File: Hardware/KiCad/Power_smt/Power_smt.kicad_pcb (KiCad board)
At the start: 2 copper layers, 38.1 x 25.4 mm, 11 parts

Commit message: power board kicad smt
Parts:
- removed @HOLE0: , 
- removed D1: 1N5819-B, switched-lm2575:DO41-7.6
- removed R1: , switched-lm2575:0207_10
- added C3: 100nF, Capacitor_SMD:C_0805_2012Metric, F.Cu at (134.6, 101.6)
- added C4: 22uF, Capacitor_SMD:C_0805_2012Metric, F.Cu at (134.6, 104.6)
- C1: value 100uF -> 10uF; footprint switched-lm2575:E2,5-6 -> Capacitor_SMD:C_0805_2012Metric
- C2: value 330uF -> 22uF; footprint switched-lm2575:E3,5-8 -> Capacitor_SMD:C_0805_2012Metric
- GND0, UNK5V0: value (none) -> 3,81/1,4
- IC1: value (none) -> LM2596TV; footprint switched-lm2575:TO220-51 -> Package_TO_SOT_SMD:TSOT-23-6
- J1: value (none) -> JACK-PLUG0; footprint switched-lm2575:SPC4077 -> Connector_BarrelJack:BarrelJack_CUI_PJ-036AH-SMT_Horizontal
- JP1: value (none) -> PINHD-1X2; footprint switched-lm2575:1X02 -> Connector_PinHeader_2.54mm:PinHeader_1x02_P2.54mm_Vertical_SMD_Pin1Right
- L1: value 470uH -> 4.7uH; footprint switched-lm2575:SMCC12 -> Inductor_SMD:L_1008_2520Metric
- moved L1 24.3 mm to (134.6, 96.5)
- moved C2 13.1 mm to (139.7, 94.0)
- moved J1 5.07 mm to (157.5, 99.1), turned to 180 degrees
- moved C1 3.99 mm to (138.4, 101.6)
- moved IC1 3.95 mm to (144.8, 96.5)
- moved JP1 2.53 mm to (144.8, 104.1)
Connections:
- IC1 pad 1: VIN -> VCC
- IC1 pad 2: N$2 -> Net-(IC1-EN)
- IC1 pad 3: GND -> Net-(IC1-EN)
- IC1 pad 4: VCC -> GND
- IC1 pad 5: N$3 -> Net-(IC1-SW)
- J1 pad 2: (no net) -> unconnected-(J1-Pad2)
- J1 pad 3: VIN -> Net-(J1-Pad3)
- JP1 pad 1: N$3 -> Net-(J1-Pad3)
- JP1 pad 2: VIN -> Net-(IC1-EN)
- L1 pad 1: N$2 -> Net-(IC1-SW)
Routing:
- net VIN: track 65.4 -> 0.00 mm
- net VCC: track 33.9 -> 61.3 mm, vias 0 -> 3
- net Net-(IC1-SW): track 0.00 -> 27.2 mm, vias 0 -> 2
- net N$2: track 17.0 -> 0.00 mm
- net Net-(J1-Pad3): track 0.00 -> 16.0 mm
- net Net-(IC1-BST): track 0.00 -> 15.8 mm, vias 0 -> 2
- net Net-(IC1-EN): track 0.00 -> 15.6 mm
- net N$3: track 5.97 -> 0.00 mm

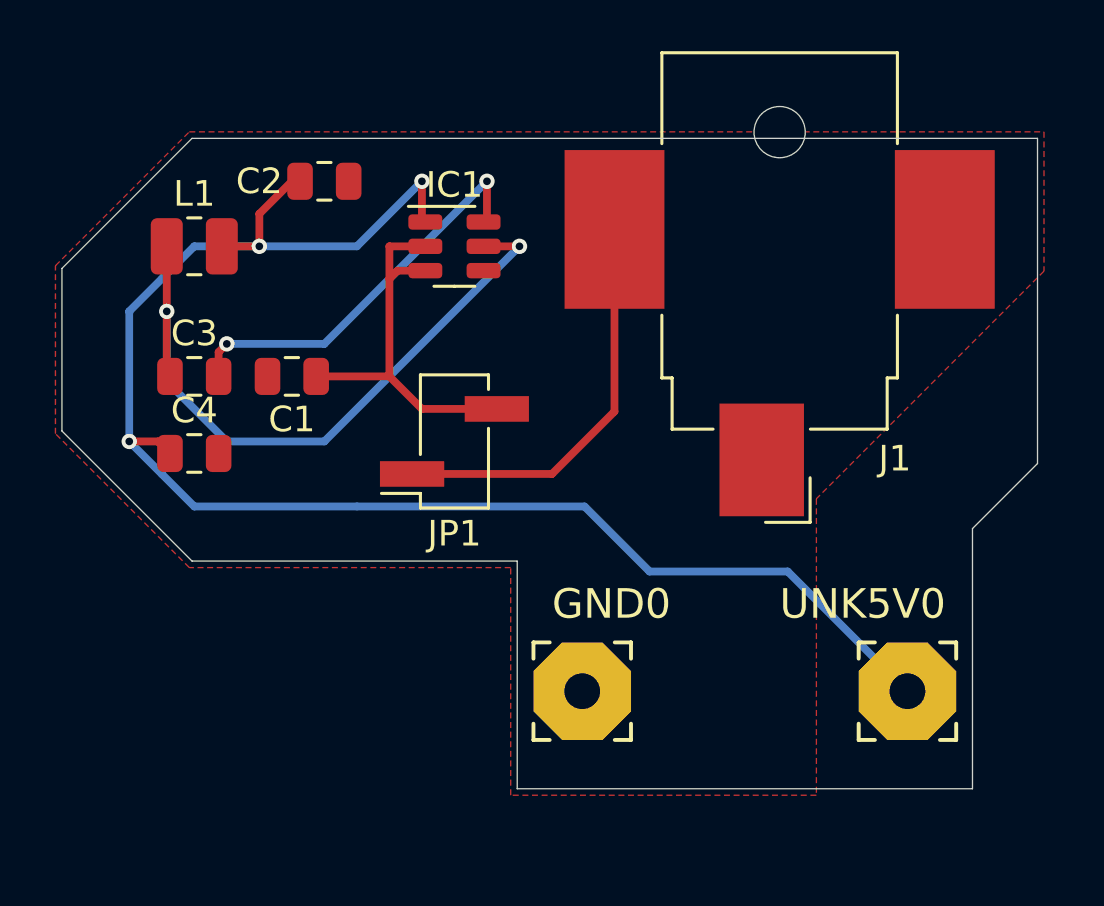
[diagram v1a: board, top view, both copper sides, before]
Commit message: SMT edits and start of fake dual ram sketching
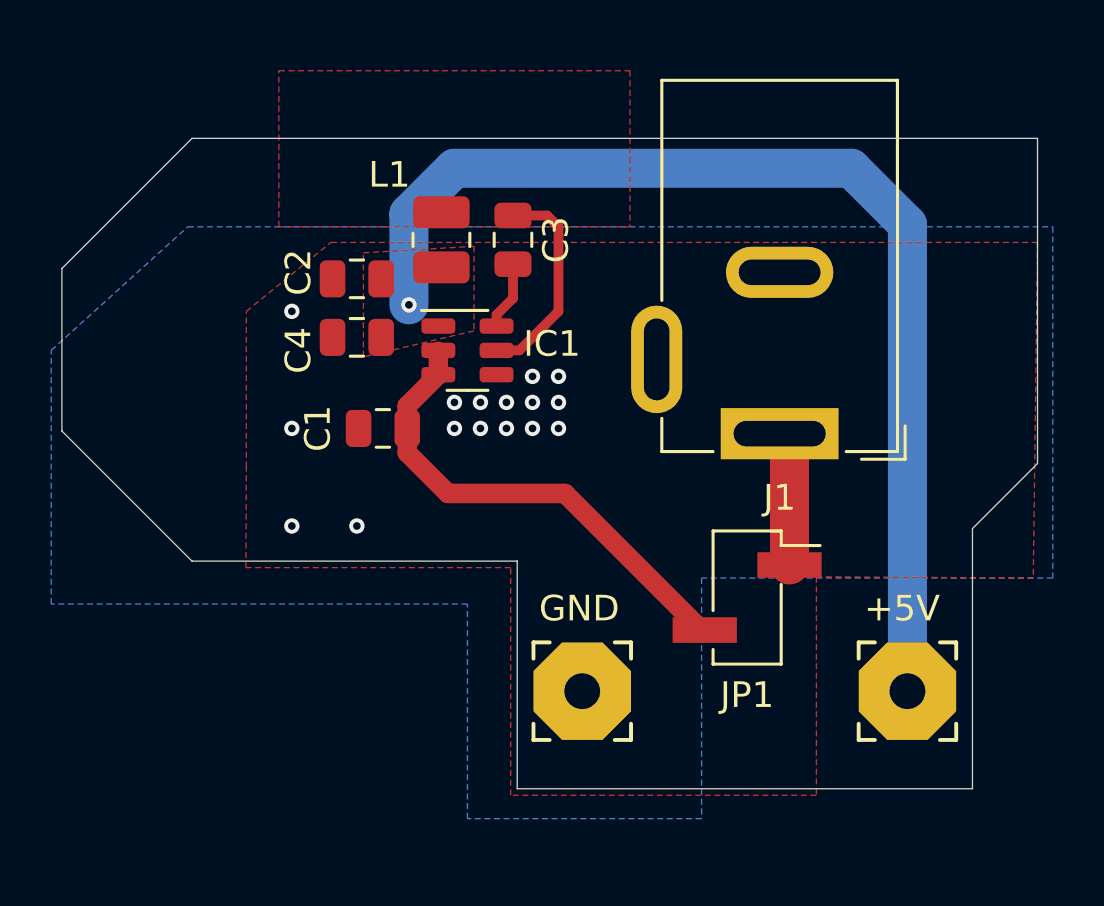
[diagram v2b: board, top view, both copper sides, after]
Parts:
- IC1: value LM2596TV -> AP63205WU-7
- J1: footprint Connector_BarrelJack:BarrelJack_CUI_PJ-036AH-SMT_Horizontal -> Connector_BarrelJack:BarrelJack_GCT_DCJ200-10-A_Horizontal
- moved C3 13.5 mm to (147.1, 96.3), turned to -90 degrees
- moved JP1 13.0 mm to (156.2, 110.2), turned to 0 degrees
- moved L1 9.66 mm to (144.3, 96.3), turned to -90 degrees
- moved C4 7.80 mm to (141.0, 100.1), turned to 180 degrees
- moved J1 4.78 mm to (157.5, 103.8)
- moved IC1 4.10 mm to (145.3, 100.6)
- moved C1 4.10 mm to (142.0, 103.6)
- moved C2 4.02 mm to (141.0, 97.8), turned to 180 degrees
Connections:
- J1 pad 1: GND -> Net-(J1-Pad1)
- J1 pad 2: unconnected-(J1-Pad2) -> GND
- J1 pad 3: Net-(J1-Pad3) -> unconnected-(J1-Pad3)
- JP1 pad 1: Net-(J1-Pad3) -> Net-(J1-Pad1)
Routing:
- net Net-(IC1-SW): track 27.2 -> 8.31 mm, vias 2 -> 0
- net VCC: track 61.3 -> 42.9 mm, vias 3 -> 1
- net Net-(J1-Pad3): track 16.0 -> 0.00 mm
- net Net-(IC1-BST): track 15.8 -> 2.68 mm, vias 2 -> 0
- net Net-(J1-Pad1): track 0.00 -> 5.29 mm
- net Net-(IC1-EN): track 15.6 -> 18.8 mm
- net GND: vias 0 -> 16
- added copper zone on B.Cu, net GND
- added copper zone on F.Cu, net Net-(IC1-SW)
- added copper zone on F.Cu, net VCC
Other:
- board text added: "+5V"
- board text added: "GND"

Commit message: updates to kicad smt versions
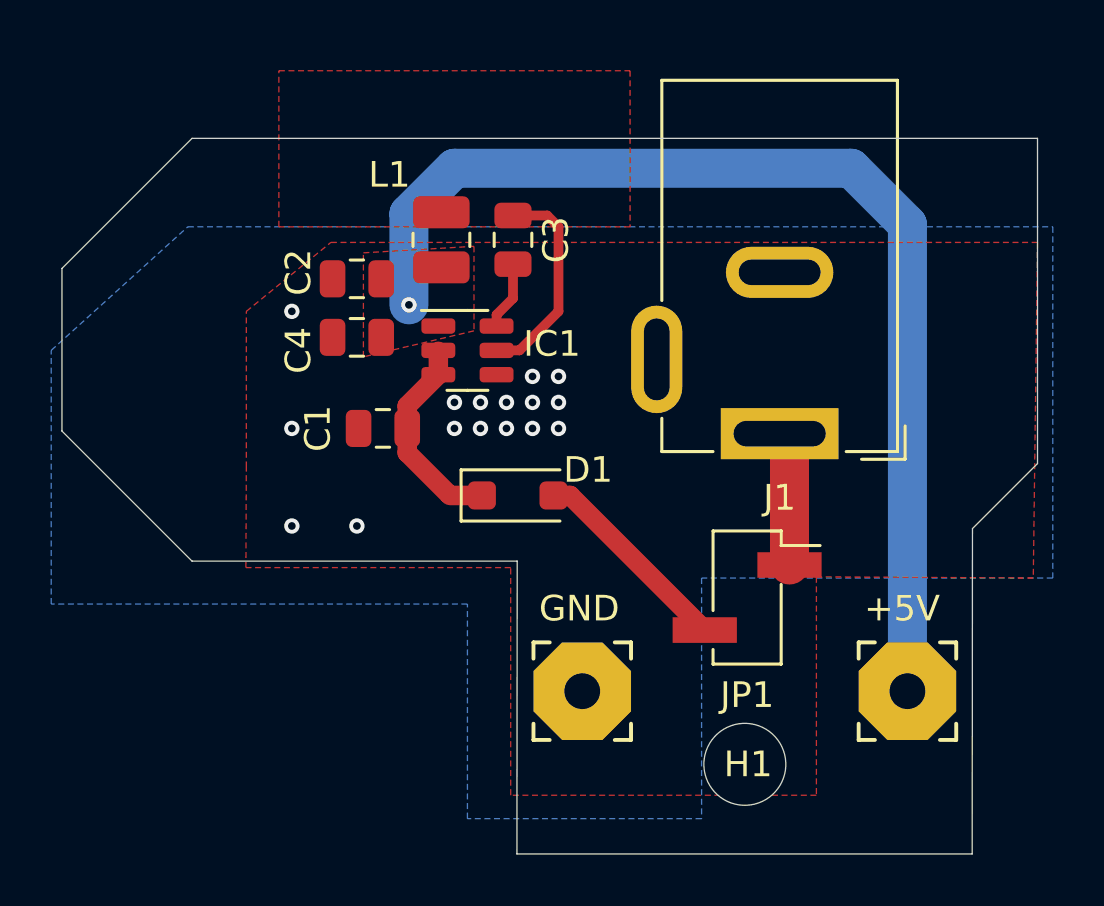
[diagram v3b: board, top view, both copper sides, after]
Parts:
- added D1: 1N4007, Diode_SMD:D_SOD-123F, F.Cu at (147.2, 106.2)
- added H1: MountingHole, MountingHole:MountingHole_3.2mm_M3, F.Cu at (156.1, 116.8)
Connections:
- C1 pad 1: Net-(IC1-EN) -> Net-(D1-K)
- IC1 pad 2: Net-(IC1-EN) -> Net-(D1-K)
- IC1 pad 3: Net-(IC1-EN) -> Net-(D1-K)
- JP1 pad 2: Net-(IC1-EN) -> Net-(D1-A)
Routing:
- net Net-(IC1-EN): track 18.8 -> 0.00 mm
- net Net-(D1-A): track 0.00 -> 8.08 mm
- net Net-(D1-K): track 0.00 -> 8.07 mm
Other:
- board size 38.1 x 25.4 mm -> 38.1 x 27.9 mm
